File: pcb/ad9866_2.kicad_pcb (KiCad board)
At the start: 4 copper layers, 50 x 50 mm, 113 parts, among them CN1 MEC6-140_CONNECTOR_BEMICRO, CON1 USB-MICRO-B, P1 CONN_2, P10 CONN_1, P2 CONN_10X2, P3 CONN_1, P4 CONN_5X2, P5 CONN_1, P5V0 CONN_1, P6 Coaxial_Connector, P7 Coaxial_Connector, P8 CONN_2, P9 CONN_1, Q1 Si2301, T1 TRANSF_ADT2, T2 TRANSF_ADT8, U1 NCP1117ST33T3G, U2 NCP1117ST33T3G, U3 Si510, U4 AD9866BCPZ, U5 NCP1117ST33T3G, U6 25AA02E48T-I/OT

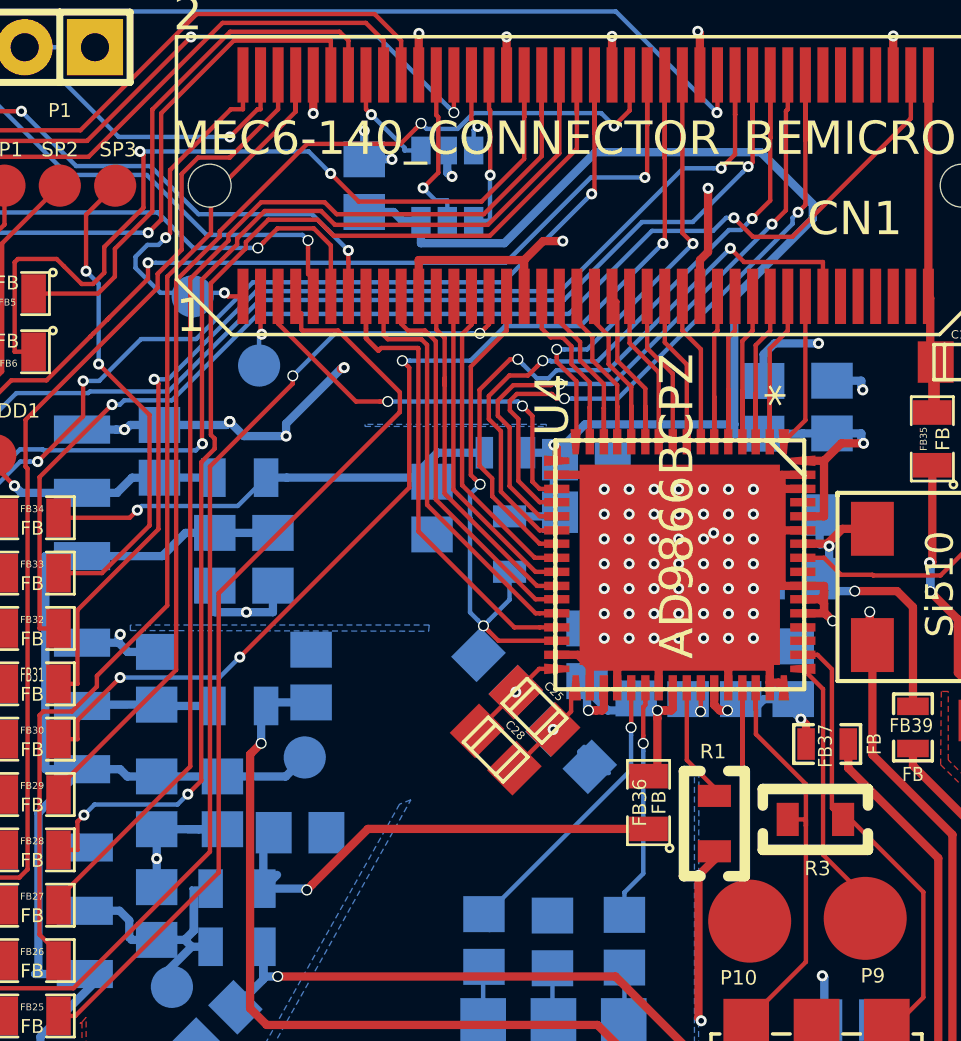
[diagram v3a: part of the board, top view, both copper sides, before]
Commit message: Routed the CLKOUT on only front side, but made a lot of vias on other signals.
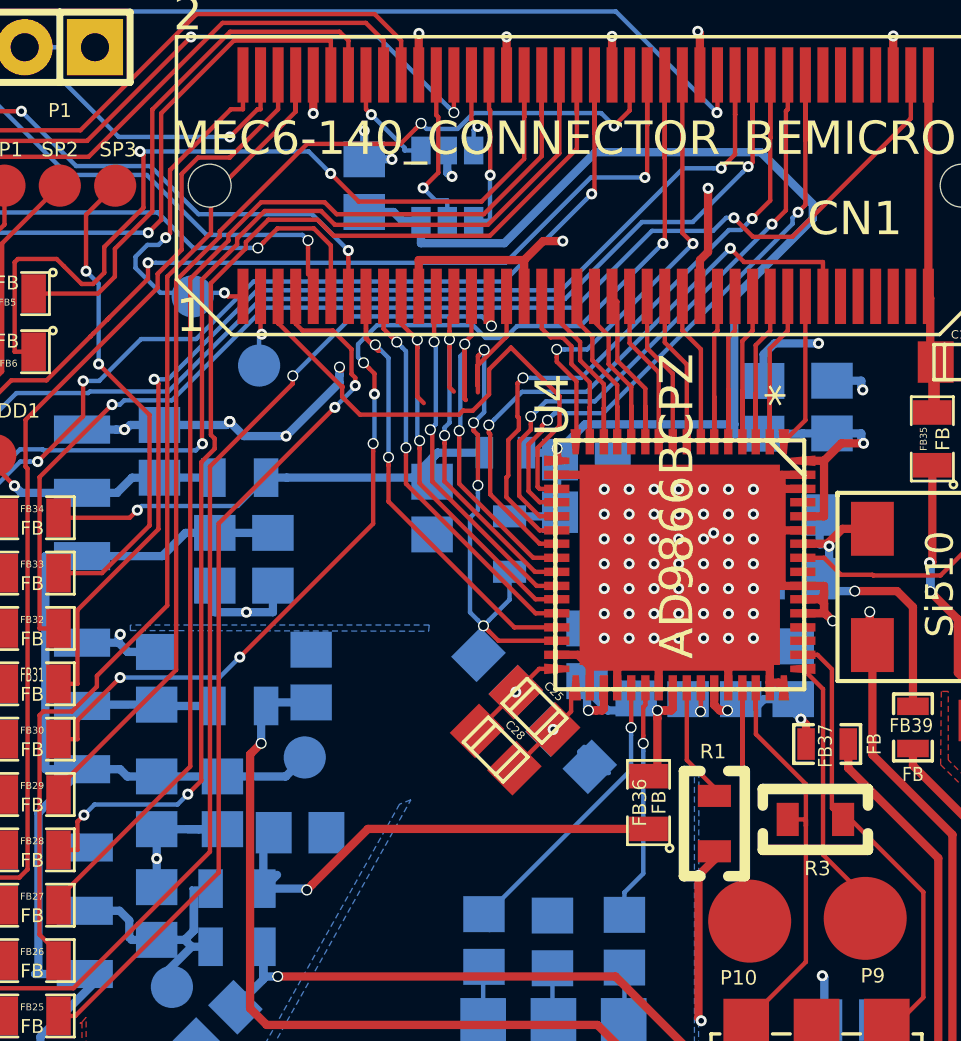
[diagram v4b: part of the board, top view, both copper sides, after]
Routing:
- net Net-(CN1-Pad5): track 15.5 -> 21.0 mm, vias 2 -> 0
- net Net-(CN1-Pad27): track 12.1 -> 16.3 mm, vias 0 -> 2
- net Net-(CN1-Pad31): track 19.1 -> 22.0 mm, vias 2 -> 4
- net Net-(CN1-Pad25): track 12.6 -> 14.8 mm, vias 0 -> 2
- net /P53: track 41.8 -> 43.9 mm, vias 4 -> 6
- net Net-(CN1-Pad19): track 14.7 -> 16.7 mm, vias 0 -> 2
- net /SDIO: track 25.7 -> 23.7 mm
- net /SEN: track 24.2 -> 22.4 mm
- net /SDO: track 24.2 -> 22.5 mm
- net /P2: track 34.5 -> 33.0 mm, vias 0 -> 2
- net /SCK: track 26.2 -> 25.3 mm
- net Net-(CN1-Pad17): track 16.0 -> 15.4 mm, vias 0 -> 2
- net Net-(CN1-Pad15): track 18.8 -> 18.4 mm, vias 0 -> 2
- net Net-(CN1-Pad23): vias 0 -> 2

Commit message: Probably abandoning this branch....
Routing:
- net GND: track 144.2 -> 172.1 mm, vias 84 -> 93
- net Net-(CN1-Pad5): track 21.0 -> 16.4 mm
- net Net-(CN1-Pad27): track 16.3 -> 12.2 mm
- net Net-(CN1-Pad19): track 16.7 -> 14.4 mm
- net Net-(CN1-Pad25): track 14.8 -> 12.8 mm
- net Net-(CN1-Pad31): track 22.0 -> 20.1 mm, vias 4 -> 2
- net Net-(CN1-Pad15): track 18.4 -> 16.6 mm
- net /P2: track 33.0 -> 31.5 mm
- net /SDO: track 22.5 -> 23.7 mm
- net /P53: track 43.9 -> 42.8 mm, vias 6 -> 4
- net /SCK: track 25.3 -> 26.3 mm
- net /SDIO: track 23.7 -> 24.7 mm
- net /SEN: track 22.4 -> 23.3 mm
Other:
- net class Default: clearance 0.155 -> 0.16
- net class GND: clearance 0.155 -> 0.16
- net class Power: clearance 0.155 -> 0.16
- rule trace_clearance: 0.155 -> 0.16
